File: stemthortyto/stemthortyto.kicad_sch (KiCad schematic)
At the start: 64 parts, among them IC1 E22-900M22S, J1 Jack-DC, Q1 BCV29, U1 LT1585-3.3, U2 ADXL343, U3 RK3588S, U4 K4UCE3Q4AB-MGCL, U5 FEMDRW032G-88A19

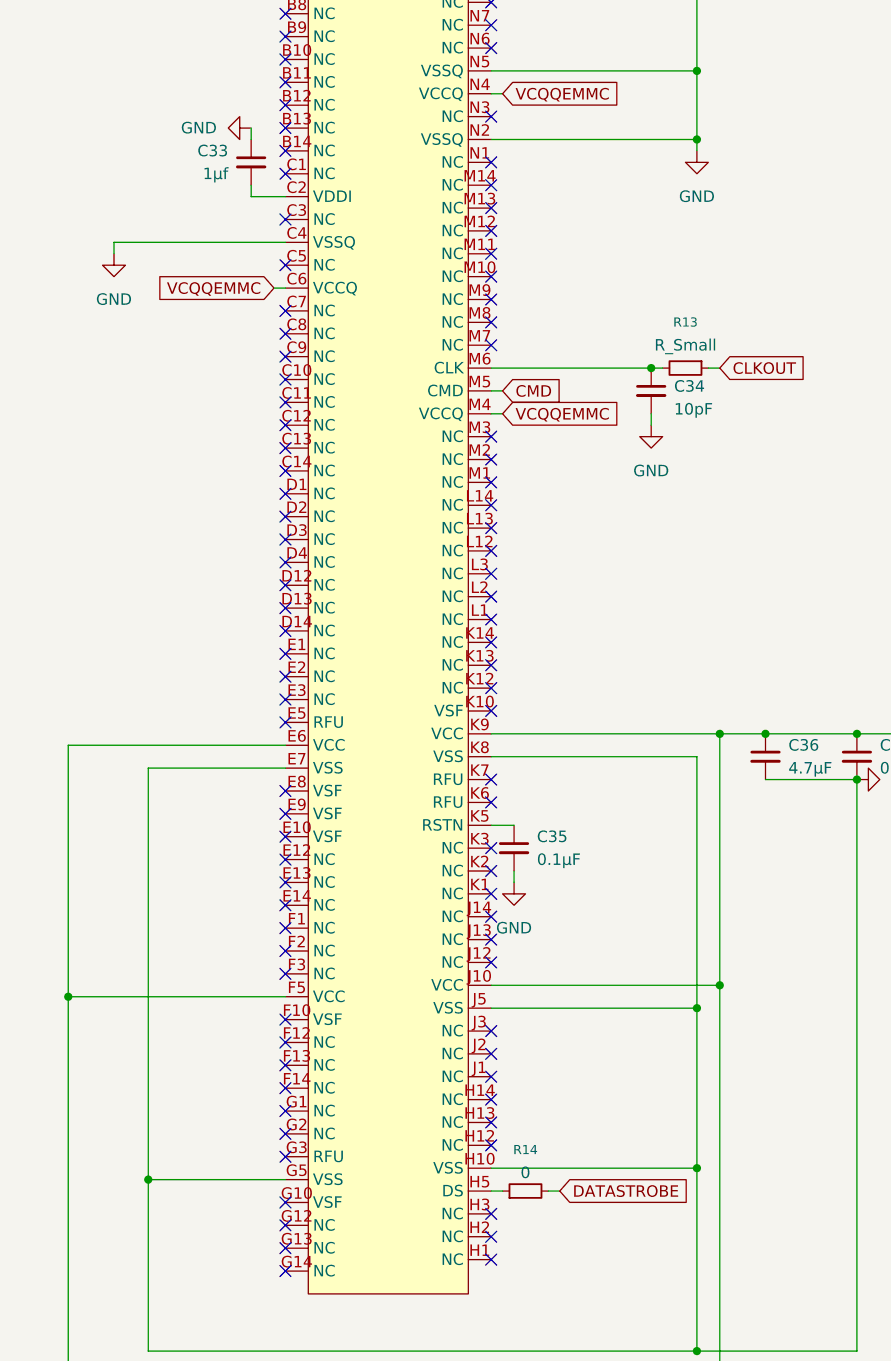
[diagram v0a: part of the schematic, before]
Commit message: Update eMMC
Updated eMMC routing removed certain resistors (0 ohm, used for jumping/ troubleshooting probably but harmful to the design)
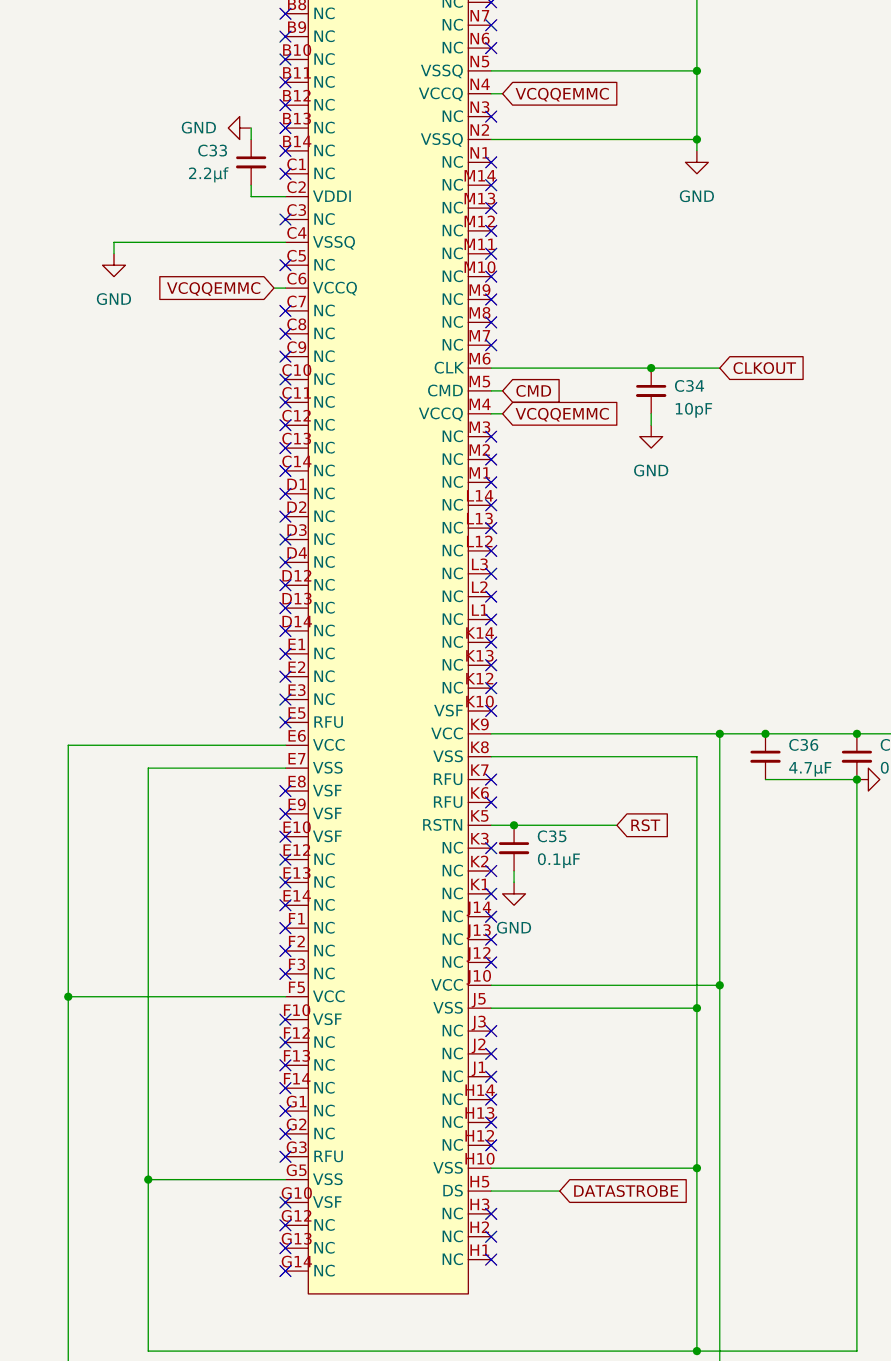
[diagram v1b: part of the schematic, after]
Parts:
- removed R13: R_Small, Resistor_SMD:R_0402_1005Metric, symbol Device:R_Small
- removed R14: 0, Resistor_SMD:R_0402_1005Metric, symbol Device:R_Small
- C33: value 1μf -> 2.2μf
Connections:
- net CLKOUT: now also C34.1, U5.M6 (CLK)
- net DATASTROBE: now also U5.H5 (DS)
- net RST: now also C35.1, U5.K5 (RSTN)
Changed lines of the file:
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@@
 	)
 	(junction
+		(at 254 320.04)
+		(diameter 0)
+		(color 0 0 0 0)
+	)
+	(junction
 		(at 274.32 203.2)
 		(diameter 0)
@@
 	(wire
 		(pts
-			(xy 257.81 360.68) (xy 259.08 360.68)
-		)
-		(stroke
-			(width 0)
-			(type default)
-		)
-	)
-	(wire
-		(pts
 			(xy 88.9 534.67) (xy 88.9 537.21)
 		)
@@
 	(wire
 		(pts
-			(xy 251.46 360.68) (xy 252.73 360.68)
+			(xy 251.46 360.68) (xy 259.08 360.68)
 		)
 		(stroke
@@
 	(wire
 		(pts
-			(xy 269.24 269.24) (xy 270.51 269.24)
+			(xy 269.24 269.24) (xy 276.86 269.24)
 		)
 		(stroke
@@
 	(wire
 		(pts
+			(xy 254 320.04) (xy 265.43 320.04)
+		)
+		(stroke
+			(width 0)
+			(type default)
+		)
+	)
+	(wire
+		(pts
 			(xy 251.46 506.73) (xy 252.73 506.73)
 		)
@@
 	(wire
 		(pts
-			(xy 275.59 269.24) (xy 276.86 269.24)
-		)
-		(stroke
-			(width 0)
-			(type default)
-		)
-	)
-	(wire
-		(pts
 			(xy 224.79 248.92) (xy 224.79 250.19)
 		)
@@
 		)
 	)
+	(global_label "RST"
+		(shape input)
+		(at 265.43 320.04 0)
+		(fields_autoplaced yes)
+		(effects
+			(font
+				(size 1.27 1.27)
+			)
+			(justify left)
+		)
+		(property "Intersheetrefs" "${INTERSHEET_REFS}"
+			(at 271.8623 320.04 0)
+			(hide yes)
+			(show_name no)
+			(do_not_autoplace no)
+			(effects
+				(font
+					(size 1.27 1.27)
+				)
+				(justify left)
+			)
+		)
+	)
 	(global_label "DAT5"
 		(shape input)
@@
 	)
 	(symbol
-		(lib_id "Device:R_Small")
-		(at 255.27 360.68 90)
-		(unit 1)
-		(body_style 1)
-		(exclude_from_sim no)
-		(in_bom yes)
-		(on_board yes)
-		(in_pos_files yes)
-		(dnp no)
-		(property "Reference" "R14"
-			(at 255.27 356.108 90)
-			(show_name no)
-			(do_not_autoplace no)
-			(effects
-				(font
-					(size 1.016 1.016)
-				)
-			)
-		)
-		(property "Value" "0"
-			(at 255.27 358.648 90)
-			(show_name no)
-			(do_not_autoplace no)
-			(effects
-				(font
-					(size 1.27 1.27)
-				)
-			)
-		)
-		(property "Footprint" "Resistor_SMD:R_0402_1005Metric"
-			(at 255.27 360.68 0)
-			(hide yes)
-			(show_name no)
-			(do_not_autoplace no)
-			(effects
-				(font
-					(size 1.27 1.27)
-				)
-			)
-		)
-		(property "Datasheet" ""
-			(at 255.27 360.68 0)
-			(hide yes)
-			(show_name no)
-			(do_not_autoplace no)
-			(effects
-				(font
-					(size 1.27 1.27)
-				)
-			)
-		)
-		(property "Description" "Resistor, small symbol"
-			(at 255.27 360.68 0)
-			(hide yes)
-			(show_name no)
-			(do_not_autoplace no)
-			(effects
-				(font
-					(size 1.27 1.27)
-				)
-			)
-		)
-		(pin "2"
-		)
-		(pin "1"
-		)
-		(instances
-			(project "stemthortyto"
-				(path "/22f1fa3f-8869-41ca-81f8-31f024e4ddf1"
-					(reference "R14")
-					(unit 1)
-				)
-			)
-		)
-	)
-	(symbol
 		(lib_id "power:+3.3V")
 		(at 375.92 234.95 0)
@@
 	)
 	(symbol
-		(lib_id "Device:R_Small")
-		(at 273.05 269.24 270)
-		(unit 1)
-		(body_style 1)
-		(exclude_from_sim no)
-		(in_bom yes)
-		(on_board yes)
-		(in_pos_files yes)
-		(dnp no)
-		(fields_autoplaced yes)
-		(property "Reference" "R13"
-			(at 273.05 264.16 90)
-			(show_name no)
-			(do_not_autoplace no)
-			(effects
-				(font
-					(size 1.016 1.016)
-				)
-			)
-		)
-		(property "Value" "R_Small"
-			(at 273.05 266.7 90)
-			(show_name no)
-			(do_not_autoplace no)
-			(effects
-				(font
-					(size 1.27 1.27)
-				)
-			)
-		)
-		(property "Footprint" "Resistor_SMD:R_0402_1005Metric"
-			(at 273.05 269.24 0)
-			(hide yes)
-			(show_name no)
-			(do_not_autoplace no)
-			(effects
-				(font
-					(size 1.27 1.27)
-				)
-			)
-		)
-		(property "Datasheet" ""
-			(at 273.05 269.24 0)
-			(hide yes)
-			(show_name no)
-			(do_not_autoplace no)
-			(effects
-				(font
-					(size 1.27 1.27)
-				)
-			)
-		)
-		(property "Description" "Resistor, small symbol"
-			(at 273.05 269.24 0)
-			(hide yes)
-			(show_name no)
-			(do_not_autoplace no)
-			(effects
-				(font
-					(size 1.27 1.27)
-				)
-			)
-		)
-		(pin "1"
-		)
-		(pin "2"
-		)
-		(instances
-			(project "stemthortyto"
-				(path "/22f1fa3f-8869-41ca-81f8-31f024e4ddf1"
-					(reference "R13")
-					(unit 1)
-				)
-			)
-		)
-	)
-	(symbol
 		(lib_id "Device:C_Small")
 		(at 127 453.39 0)
@@
 			)
 		)
-		(property "Value" "1μf"
+		(property "Value" "2.2μf"
 			(at 222.25 247.6562 0)
 			(show_name no)
